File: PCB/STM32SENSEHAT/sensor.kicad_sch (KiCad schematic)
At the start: 35 parts, among them J10 Conn_01x01_Pin, J11 Conn_01x02_Pin, J12 Conn_01x04_Pin, J13 Conn_01x04_Pin, U4 BME280, U6 LTR-303ALS-01

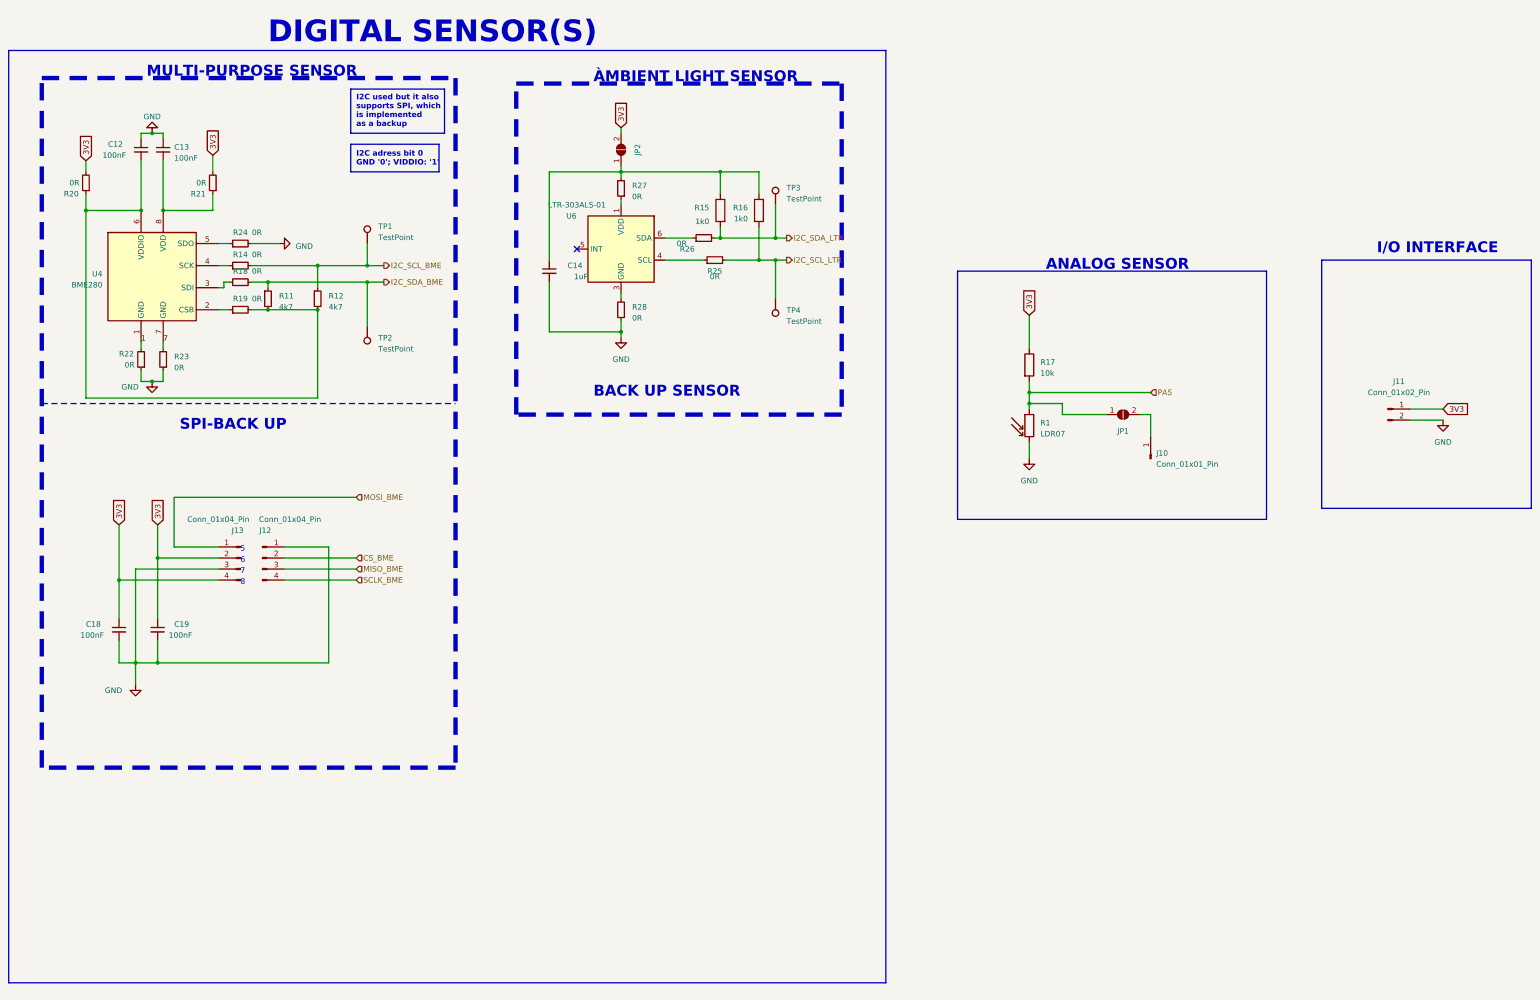
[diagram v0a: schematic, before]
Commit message: Rework of Power,MCU and Sensor Schematic
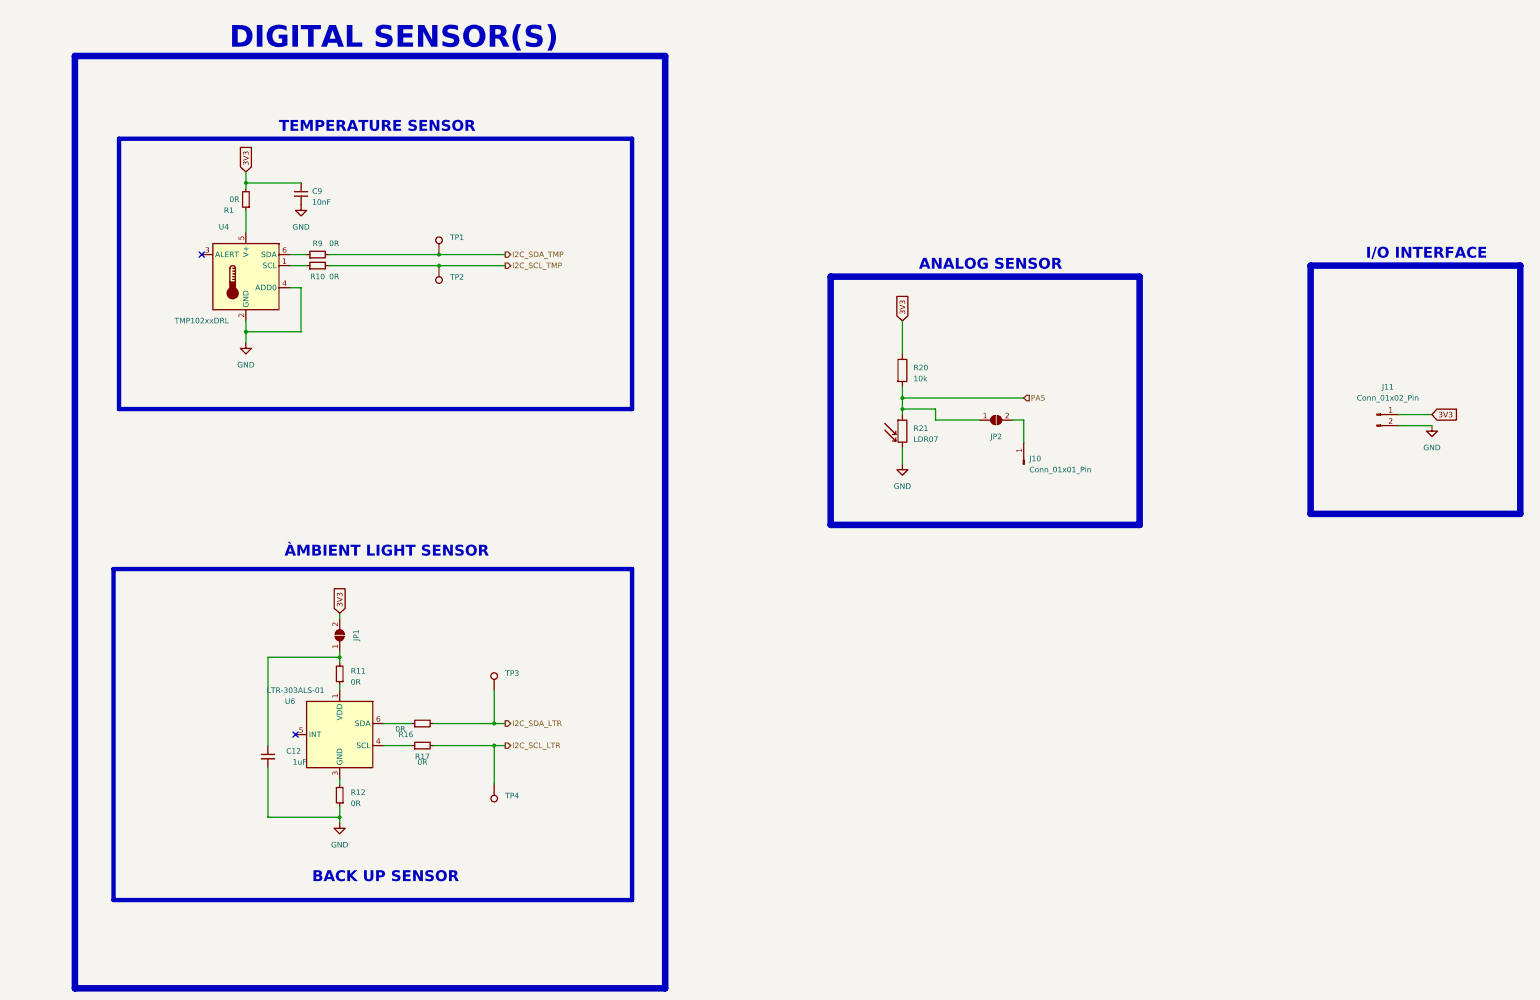
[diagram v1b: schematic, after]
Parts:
- removed C13, C18, C19: 100nF, Capacitor_SMD:C_0805_2012Metric, symbol Device:C_Small
- removed C14: 1uF, Capacitor_SMD:C_0805_2012Metric, symbol Device:C_Small
- removed J12, J13: Conn_01x04_Pin, Connector_PinHeader_2.54mm:PinHeader_1x04_P2.54mm_Vertical, symbol Connector:Conn_01x04_Pin
- removed R1: LDR07, OptoDevice:R_LDR_5.1x4.3mm_P3.4mm_Vertical, symbol Sensor_Optical:LDR07
- removed R14, R18, R19, R20, R21, R22, R23, R24, R25, R26, R27, R28: 0R, Resistor_SMD:R_0805_2012Metric, symbol Device:R_Small
- removed R15, R16: 1k0, Resistor_SMD:R_0603_1608Metric, symbol Device:R
- removed R17: 10k, Resistor_SMD:R_0805_2012Metric, symbol Device:R
- removed U4: BME280, Package_LGA:Bosch_LGA-8_2.5x2.5mm_P0.65mm_ClockwisePinNumbering, symbol Sensor:BME280
- added C9: 10nF, JLCfootprint:C0805, symbol Device:C_Small
- added R1, R10, R16, R17, R9: 0R, JLCfootprint:R0805, symbol Device:R_Small
- added R20: 10k, JLCfootprint:R0805, symbol Device:R
- added R21: LDR07, Resistor_THT:R_Axial_DIN0204_L3.6mm_D1.6mm_P7.62mm_Horizontal, symbol Sensor_Optical:LDR07
- added U4: TMP102xxDRL, JLCfootprint:SOT-563_L1.6-W1.2-P0.50-LS1.6-BR, symbol Sensor_Temperature:TMP102xxDRL
- C12: value 100nF -> 1uF; footprint Capacitor_SMD:C_0805_2012Metric -> JLCfootprint:C0805
- JP1: footprint Jumper:SolderJumper-2_P1.3mm_Open_RoundedPad1.0x1.5mm -> Jumper:SolderJumper-2_P1.3mm_Open_Pad1.0x1.5mm
- JP2: footprint Jumper:SolderJumper-2_P1.3mm_Open_Pad1.0x1.5mm -> Jumper:SolderJumper-2_P1.3mm_Open_RoundedPad1.0x1.5mm
- R11, R12: value 4k7 -> 0R; footprint Resistor_SMD:R_0805_2012Metric -> JLCfootprint:R0805
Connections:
- net 3V3: now also JP1.2 (B), C9.1, R1.2, R20.1; no longer JP2.2 (B)
- net GND: now also C12.2, R12.1, C9.2, R21.2, U4.2 (GND), U4.4 (ADD0); no longer C12.1
- net I2C_SCL_LTR: now also R17.2
- net I2C_SDA_LTR: now also R16.2
- net PA5: now also JP2.1 (A), R20.2, R21.1; no longer JP1.1 (A)
- net at U6.6 (SDA): now also R16.1
- net at J10.1 (Pin_1): now also JP2.2 (B); no longer JP1.2 (B)
- net at U6.1 (VDD): now also R11.1
- net at U6.3 (GND): now also R12.2
- net at U6.4 (SCL): now also R17.1
- net I2C_SCL_BME renamed I2C_SDA_TMP
- net I2C_SDA_TMP: now also R9.2; no longer R12.1
- net I2C_SDA_BME renamed I2C_SCL_TMP
- net I2C_SCL_TMP: now also R10.2; no longer R11.1
- new net: C12.1, JP1.1 (A), R11.2
- new net: R1.1, U4.5 (V+)
- new net: R9.1, U4.6 (SDA)
- new net: R10.1, U4.1 (SCL)
- no-connect marks 1 -> 2
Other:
- note added: "TEMPERATURE SENSOR"
- note removed: "5"
- note removed: "6"
- note removed: "7"
- note removed: "8"
- note removed: "I2C adress bit 0 GND '0'; VIDDIO: '1'"
- note removed: "I2C used but it also supports SPI, which is implemented as a backup"
- note removed: "MULTI-PURPOSE SENSOR"
- note removed: "SPI-BACK UP"

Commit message: PCB draft
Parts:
- C12, C9: footprint JLCfootprint:C0805 -> Capacitor_SMD:C_0805_2012Metric
- R1, R10, R11, R12, R16, R17, R20, R9: footprint JLCfootprint:R0805 -> Resistor_SMD:R_0805_2012Metric
- R21: footprint Resistor_THT:R_Axial_DIN0204_L3.6mm_D1.6mm_P7.62mm_Horizontal -> OptoDevice:R_LDR_5.1x4.3mm_P3.4mm_Vertical
- U6: footprint OptoDevice:Lite-On_LTR-303ALS-01 -> JLCfootprint:SOT-363_L2.0-W1.3-P0.65-LS2.1-BL
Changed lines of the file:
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@@
       (effects (font (size 1.27 1.27)) (justify right))
     )
-    (property "Footprint" "JLCfootprint:R0805" (at 104.14 184.15 0)
+    (property "Footprint" "Resistor_SMD:R_0805_2012Metric" (at 104.14 184.15 0)
       (effects (font (size 1.27 1.27)) hide)
     )
@@
       (effects (font (size 1.27 1.27)))
     )
-    (property "Footprint" "JLCfootprint:R0805" (at 123.19 195.58 0)
+    (property "Footprint" "Resistor_SMD:R_0805_2012Metric" (at 123.19 195.58 0)
       (effects (font (size 1.27 1.27)) hide)
     )
@@
       (effects (font (size 1.27 1.27)) (justify right))
     )
-    (property "Footprint" "JLCfootprint:R0805" (at 82.55 74.93 0)
+    (property "Footprint" "Resistor_SMD:R_0805_2012Metric" (at 82.55 74.93 0)
       (effects (font (size 1.27 1.27)) hide)
     )
@@
       (effects (font (size 1.27 1.27)))
     )
-    (property "Footprint" "JLCfootprint:R0805" (at 99.06 87.63 0)
+    (property "Footprint" "Resistor_SMD:R_0805_2012Metric" (at 99.06 87.63 0)
       (effects (font (size 1.27 1.27)) hide)
     )
@@
       (effects (font (size 1.27 1.27)) (justify left))
     )
-    (property "Footprint" "JLCfootprint:C0805" (at 87.63 203.2 0)
+    (property "Footprint" "Capacitor_SMD:C_0805_2012Metric" (at 87.63 203.2 0)
       (effects (font (size 1.27 1.27)) hide)
     )
@@
       (effects (font (size 1.27 1.27)) (justify left))
     )
-    (property "Footprint" "JLCfootprint:R0805" (at 231.902 114.3 90)
+    (property "Footprint" "Resistor_SMD:R_0805_2012Metric" (at 231.902 114.3 90)
       (effects (font (size 1.27 1.27)) hide)
     )
@@
       (effects (font (size 1.27 1.27)) (justify right))
     )
-    (property "Footprint" "JLCfootprint:R0805" (at 104.14 212.09 0)
+    (property "Footprint" "Resistor_SMD:R_0805_2012Metric" (at 104.14 212.09 0)
       (effects (font (size 1.27 1.27)) hide)
     )
@@
       (effects (font (size 1.27 1.27)))
     )
-    (property "Footprint" "JLCfootprint:R0805" (at 123.19 200.66 0)
+    (property "Footprint" "Resistor_SMD:R_0805_2012Metric" (at 123.19 200.66 0)
       (effects (font (size 1.27 1.27)) hide)
     )
@@
       (effects (font (size 1.27 1.27)) (justify left))
     )
-    (property "Footprint" "Resistor_THT:R_Axial_DIN0204_L3.6mm_D1.6mm_P7.62mm_Horizontal" (at 238.125 128.27 90)
+    (property "Footprint" "OptoDevice:R_LDR_5.1x4.3mm_P3.4mm_Vertical" (at 238.125 128.27 90)
       (effects (font (size 1.27 1.27)) hide)
     )
@@
       (effects (font (size 1.27 1.27)))
     )
-    (property "Footprint" "JLCfootprint:R0805" (at 99.06 90.17 0)
+    (property "Footprint" "Resistor_SMD:R_0805_2012Metric" (at 99.06 90.17 0)
       (effects (font (size 1.27 1.27)) hide)
     )
@@
       (effects (font (size 1.27 1.27)) (justify left))
     )
-    (property "Footprint" "JLCfootprint:C0805" (at 95.25 73.66 0)
+    (property "Footprint" "Capacitor_SMD:C_0805_2012Metric" (at 95.25 73.66 0)
       (effects (font (size 1.27 1.27)) hide)
     )
@@
       (effects (font (size 1.27 1.27)))
     )
-    (property "Footprint" "OptoDevice:Lite-On_LTR-303ALS-01" (at 104.14 186.69 0)
-      (effects (font (size 1.27 1.27)) hide)
-    )
+    (property "Footprint" "JLCfootprint:SOT-363_L2.0-W1.3-P0.65-LS2.1-BL" (at 104.14 186.69 0)
+      (effects (font (size 1.27 1.27)) hide)
+    )

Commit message: Changed TMP102 capacitor footprint to ceramic
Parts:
- C9: footprint Capacitor_SMD:C_0805_2012Metric -> Capacitor_THT:C_Disc_D5.0mm_W2.5mm_P5.00mm
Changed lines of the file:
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@@
       (effects (font (size 1.27 1.27)) (justify left))
     )
-    (property "Footprint" "Capacitor_SMD:C_0805_2012Metric" (at 95.25 73.66 0)
+    (property "Footprint" "Capacitor_THT:C_Disc_D5.0mm_W2.5mm_P5.00mm" (at 95.25 73.66 0)
       (effects (font (size 1.27 1.27)) hide)
     )
